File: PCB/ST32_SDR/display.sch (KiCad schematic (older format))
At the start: 24 parts, among them J2 IDC10 Serial Wire, Q7 BC817, SW1 SW_Push_Dual, SW2 SW_Push_Dual, SW3 SW_Push_Dual, SW4 SW_Push_Dual, SW5 ENCODER, SW6 SW_Push_Dual, U15 Nokia_5110_LCD

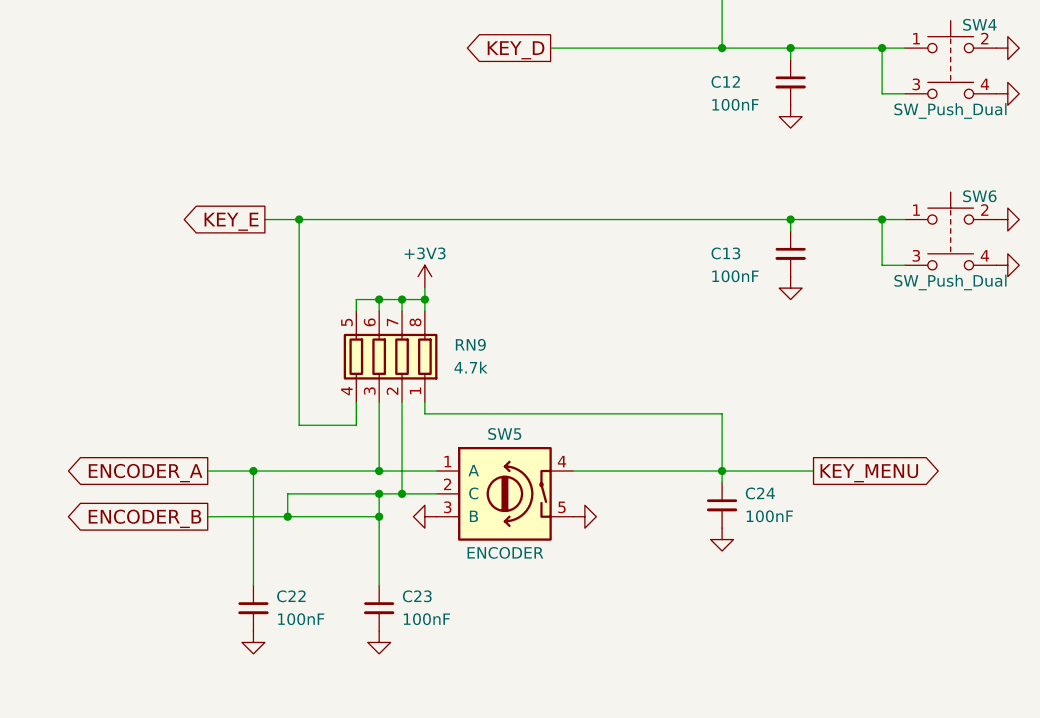
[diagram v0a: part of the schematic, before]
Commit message: PCB Linux 2, update AUDIO_OUT
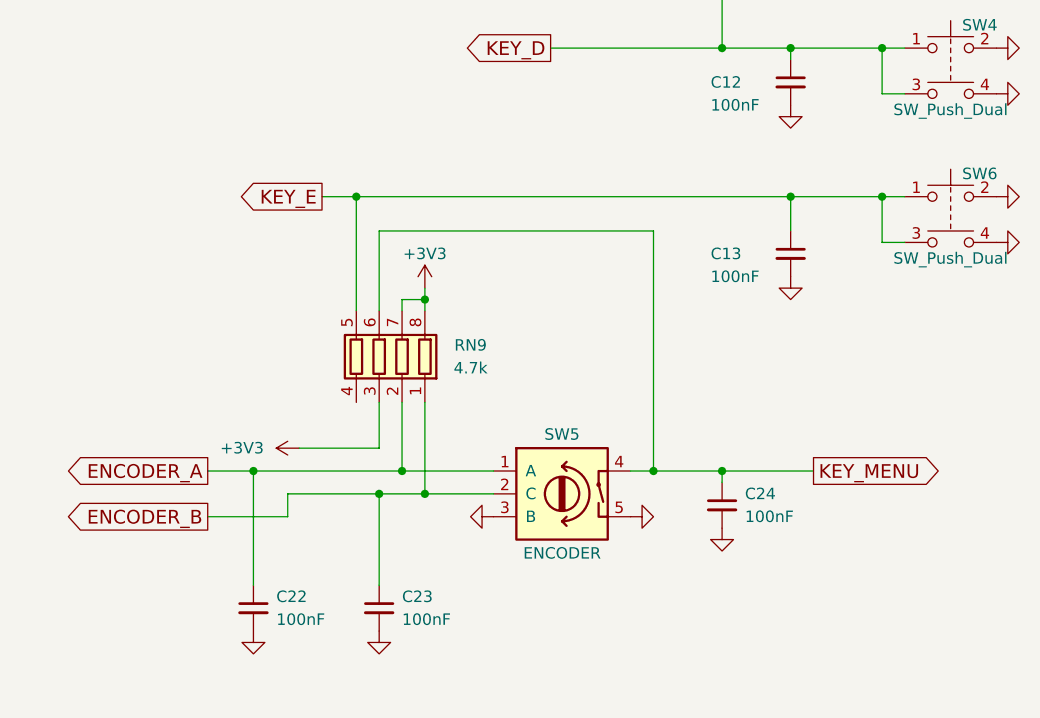
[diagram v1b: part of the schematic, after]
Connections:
- net +3V3: now also RN9.3 (R3.1); no longer RN9.5 (R4.2), RN9.6 (R3.2)
- net ENCODER_A: now also RN9.2 (R2.1); no longer RN9.3 (R3.1)
- net ENCODER_B: now also RN9.1 (R1.1); no longer RN9.2 (R2.1)
- net KEY_E: now also RN9.5 (R4.2); no longer RN9.4 (R4.1)
- net KEY_MENU: now also RN9.6 (R3.2); no longer RN9.1 (R1.1)
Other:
- moved on the sheet: SW5, SW6
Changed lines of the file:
@@
 LIBS:4ms-ic
 LIBS:Display
-LIBS:switches
-LIBS:cmos4000
+LIBS:Connector
+LIBS:Relay
 LIBS:LCSDR-cache
 EELAYER 25 0
@@
 L Rotary_Encoder_Switch SW5
 U 1 1 5DDEFBA4
-P 8100 5650
-F 0 "SW5" H 8100 5910 50  0000 C CNN
-F 1 "ENCODER" H 8100 5390 50  0000 C CNN
-F 2 "UI:SF-ROTARY-ENCODER" H 8000 5810 50  0001 C CNN
-F 3 "" H 8100 5910 50  0001 C CNN
-	1    8100 5650
+P 8350 5650
+F 0 "SW5" H 8350 5910 50  0000 C CNN
+F 1 "ENCODER" H 8350 5390 50  0000 C CNN
+F 2 "UI:SF-ROTARY-ENCODER" H 8250 5810 50  0001 C CNN
+F 3 "" H 8350 5910 50  0001 C CNN
+	1    8350 5650
 	1    0    0    -1
 $EndComp
@@
 L GND #PWR074
 U 1 1 5DDEFDCD
-P 8400 5750
-F 0 "#PWR074" H 8400 5500 50  0001 C CNN
-F 1 "GND" H 8400 5600 50  0001 C CNN
-F 2 "" H 8400 5750 50  0001 C CNN
-F 3 "" H 8400 5750 50  0001 C CNN
-	1    8400 5750
-	0    -1   -1   0
-$EndComp
-Wire Wire Line
-	8400 5550 9450 5550
+P 8650 5750
+F 0 "#PWR074" H 8650 5500 50  0001 C CNN
+F 1 "GND" H 8650 5600 50  0001 C CNN
+F 2 "" H 8650 5750 50  0001 C CNN
+F 3 "" H 8650 5750 50  0001 C CNN
+	1    8650 5750
+	0    -1   -1   0
+$EndComp
+Wire Wire Line
+	8650 5550 9450 5550
 $Comp
 L +3V3 #PWR075
@@
 	1    0    0    -1
 $EndComp
-Wire Wire Line
-	9050 5300 9050 5600
 Connection ~ 9050 5550
 $Comp
@@
 ENCODER_A
 Wire Wire Line
-	6800 5550 7800 5550
+	6800 5550 8050 5550
 Text GLabel 6800 5750 0    60   Output ~ 0
 ENCODER_B
-Wire Wire Line
-	7550 5750 6800 5750
 $Comp
 L GND #PWR077
 U 1 1 5DDF65E7
-P 7800 5750
-F 0 "#PWR077" H 7800 5500 50  0001 C CNN
-F 1 "GND" H 7800 5600 50  0001 C CNN
-F 2 "" H 7800 5750 50  0001 C CNN
-F 3 "" H 7800 5750 50  0001 C CNN
-	1    7800 5750
+P 8050 5750
+F 0 "#PWR077" H 8050 5500 50  0001 C CNN
+F 1 "GND" H 8050 5600 50  0001 C CNN
+F 2 "" H 8050 5750 50  0001 C CNN
+F 3 "" H 8050 5750 50  0001 C CNN
+	1    8050 5750
 	0    1    1    0
 $EndComp
@@
 $EndComp
 Wire Wire Line
-	7750 5250 7750 5300
-Wire Wire Line
-	7750 5300 9050 5300
-Wire Wire Line
 	7750 4750 7750 4850
 Wire Wire Line
-	7150 5650 7800 5650
+	7150 5650 8050 5650
 $Comp
 L GND #PWR078
@@
 $EndComp
 Wire Wire Line
-	7550 4850 7550 4800
-Wire Wire Line
-	7450 4800 7750 4800
+	7550 4500 7550 4850
 Connection ~ 7750 4800
 Wire Wire Line
 	7650 4850 7650 4800
-Connection ~ 7650 4800
 $Comp
 L C_Small C23
@@
 L SW_Push_Dual SW6
 U 1 1 5DE25B2C
-P 10050 4450
-F 0 "SW6" H 10100 4550 50  0000 L CNN
-F 1 "SW_Push_Dual" H 10050 4180 50  0000 C CNN
-F 2 "Buttons_Switches_ThroughHole:SW_PUSH_6mm_h13mm" H 10050 4650 50  0001 C CNN
-F 3 "" H 10050 4650 50  0001 C CNN
-	1    10050 4450
+P 10050 4350
+F 0 "SW6" H 10100 4450 50  0000 L CNN
+F 1 "SW_Push_Dual" H 10050 4080 50  0000 C CNN
+F 2 "Buttons_Switches_ThroughHole:SW_PUSH_6mm_h13mm" H 10050 4550 50  0001 C CNN
+F 3 "" H 10050 4550 50  0001 C CNN
+	1    10050 4350
 	1    0    0    -1
 $EndComp
@@
 	1    0    0    -1
 $EndComp
-Wire Wire Line
-	7450 4850 7450 4800
-Connection ~ 7550 4800
-Wire Wire Line
-	7450 5250 7450 5350
-Wire Wire Line
-	7450 5350 7200 5350
-Wire Wire Line
-	7200 5350 7200 4450
-Wire Wire Line
-	7050 4450 9850 4450
 $Comp
 L GND #PWR080
 U 1 1 5DE26007
-P 10250 4450
-F 0 "#PWR080" H 10250 4200 50  0001 C CNN
-F 1 "GND" H 10250 4300 50  0001 C CNN
-F 2 "" H 10250 4450 50  0001 C CNN
-F 3 "" H 10250 4450 50  0001 C CNN
-	1    10250 4450
+P 10250 4350
+F 0 "#PWR080" H 10250 4100 50  0001 C CNN
+F 1 "GND" H 10250 4200 50  0001 C CNN
+F 2 "" H 10250 4350 50  0001 C CNN
+F 3 "" H 10250 4350 50  0001 C CNN
+	1    10250 4350
 	0    -1   -1   0
 $EndComp
@@
 L GND #PWR081
 U 1 1 5DE2605A
-P 10250 4650
-F 0 "#PWR081" H 10250 4400 50  0001 C CNN
-F 1 "GND" H 10250 4500 50  0001 C CNN
-F 2 "" H 10250 4650 50  0001 C CNN
-F 3 "" H 10250 4650 50  0001 C CNN
-	1    10250 4650
-	0    -1   -1   0
-$EndComp
-Wire Wire Line
-	9850 4650 9750 4650
-Wire Wire Line
-	9750 4650 9750 4450
-Connection ~ 9750 4450
-Text GLabel 7050 4450 0    60   Output ~ 0
+P 10250 4550
+F 0 "#PWR081" H 10250 4300 50  0001 C CNN
+F 1 "GND" H 10250 4400 50  0001 C CNN
+F 2 "" H 10250 4550 50  0001 C CNN
+F 3 "" H 10250 4550 50  0001 C CNN
+	1    10250 4550
+	0    -1   -1   0
+$EndComp
+Text GLabel 7300 4350 0    60   Output ~ 0
 KEY_E
-Connection ~ 7200 4450
 $Comp
 L GND #PWR082
@@
 	1    0    0    -1
 $EndComp
-Wire Wire Line
-	9350 4500 9350 4450
-Connection ~ 9350 4450
 $Comp
 L C_Small C12
@@
 $EndComp
 Wire Wire Line
-	7650 5250 7650 5650
-Connection ~ 7650 5650
-Wire Wire Line
-	7550 5650 7550 6050
-Wire Wire Line
-	7550 5550 7550 5250
-Connection ~ 7550 5550
-Connection ~ 7550 5750
-Wire Wire Line
 	7150 5650 7150 5750
-Connection ~ 7150 5750
+Wire Wire Line
+	7650 5250 7650 5550
+Connection ~ 7650 5550
+Wire Wire Line
+	7750 5250 7750 5650
+Connection ~ 7750 5650
+Wire Wire Line
+	7150 5750 6800 5750
+Wire Wire Line
+	7550 6050 7550 5650
 Connection ~ 7550 5650
+Wire Wire Line
+	7650 4800 7750 4800
+Wire Wire Line
+	7550 4500 8750 4500
+Wire Wire Line
+	8750 4500 8750 5550
+Connection ~ 8750 5550
+Wire Wire Line
+	9050 5550 9050 5600
+$Comp
+L +3V3 #PWR083
+U 1 1 5DE4A858
+P 7200 5450
+F 0 "#PWR083" H 7200 5300 50  0001 C CNN
+F 1 "+3V3" V 7200 5700 50  0000 C CNN
+F 2 "" H 7200 5450 50  0001 C CNN
+F 3 "" H 7200 5450 50  0001 C CNN
+	1    7200 5450
+	0    -1   -1   0
+$EndComp
+Wire Wire Line
+	7200 5450 7550 5450
+Wire Wire Line
+	7550 5450 7550 5250
+Wire Wire Line
+	7450 4350 7450 4850
+Wire Wire Line
+	7300 4350 9850 4350
+Wire Wire Line
+	9850 4550 9750 4550
+Wire Wire Line
+	9750 4550 9750 4350
+Connection ~ 9750 4350
+Wire Wire Line
+	9350 4500 9350 4350
+Connection ~ 9350 4350
+Connection ~ 7450 4350
 $EndSCHEMATC
